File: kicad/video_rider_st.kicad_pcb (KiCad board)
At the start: 2 copper layers, 34 parts, among them J1 Conn_01x16_Female, J2 F3311A7H121020E200, J3 F3311A7H121020E200, J4 Conn_01x02_Male, J5 Conn_01x03_Male, J6 F3311A7H121020E200, J7 F3311A7H121020E200, J8 Conn_01x06_Male, U1 ST_SHIFTER_PHY, U10 ST_GLUE_PHY, U11 ST_GLUE_SOCKET, U2 ST_SHIFTER_SOCKET, U3 Pico, U4 74HC245, U5 74HC245, U6 74HC245, U7 74HC245, U8 LM1117-3.3, U9 XC95144XL-TQ100, X1 CXO_DIP14

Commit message: More layout experimentation
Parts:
- moved U6 37.0 mm to (185.2, 72.9)
- moved U7 23.1 mm to (177.3, 72.9)
- moved U2 8.60 mm to (198.2, 51.8)
- moved U4 3.76 mm to (155.8, 72.9)
- moved U5 3.55 mm to (163.7, 72.9)
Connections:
- net Net-(J5-Pad1) renamed /R_STE
- net Net-(J5-Pad2) renamed /G_STE
- net Net-(J5-Pad3) renamed /B_STE
- U6 pad 11: /B_OUT2 -> Net-(R2-Pad1)
- U6 pad 12: /B_OUT1 -> Net-(R3-Pad1)
- U6 pad 13: /B_OUT0 -> Net-(R4-Pad1)
- U6 pad 14: Net-(R3-Pad1) -> unconnected-(U6-Pad14)
- U6 pad 15: /G_OUT2 -> unconnected-(U6-Pad15)
- U6 pad 16: /G_OUT1 -> /B_OUT0
- U6 pad 17: /G_OUT0 -> /B_OUT1
- U6 pad 18: Net-(R2-Pad1) -> /B_OUT2
- U6 pad 2: /PICOG0 -> /PICOB3
- U6 pad 3: /PICOG1 -> /PICOB2
- U6 pad 4: /PICOG2 -> /PICOB1
- U6 pad 5: /PICOG3 -> unconnected-(U6-Pad5)
- U6 pad 6: /PICOB0 -> unconnected-(U6-Pad6)
- U6 pad 7: /PICOB1 -> /PICOB0
- U6 pad 8: /PICOB2 -> /PICOG0
- U6 pad 9: /PICOB3 -> /PICOR0
- U7 pad 11: unconnected-(U7-Pad11) -> /R_OUT0
- U7 pad 12: unconnected-(U7-Pad12) -> /R_OUT1
- U7 pad 13: unconnected-(U7-Pad13) -> /R_OUT2
- U7 pad 14: unconnected-(U7-Pad14) -> /G_OUT0
- U7 pad 15: /R_OUT2 -> /G_OUT1
- U7 pad 16: /R_OUT1 -> /G_OUT2
- U7 pad 17: /R_OUT0 -> unconnected-(U7-Pad17)
- U7 pad 18: Net-(R4-Pad1) -> unconnected-(U7-Pad18)
- U7 pad 19: /~{PICOEN_P} -> unconnected-(U7-Pad19)
- U7 pad 2: /PICOR0 -> unconnected-(U7-Pad2)
- U7 pad 3: /PICOR1 -> unconnected-(U7-Pad3)
- U7 pad 4: /PICOR2 -> /PICOG3
- U7 pad 5: /PICOR3 -> /PICOG2
- U7 pad 6: Net-(R1-Pad2) -> /PICOG1
- U7 pad 7: Net-(R1-Pad2) -> /PICOR3
- U7 pad 8: Net-(R1-Pad2) -> /PICOR2
- U7 pad 9: Net-(R1-Pad2) -> /PICOR1
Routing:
- net /G_OUT2: track 8.24 -> 28.9 mm
- net /B_OUT2: track 27.1 -> 47.7 mm
- net /G_OUT1: track 9.73 -> 27.1 mm
- net /B_OUT1: track 27.0 -> 43.4 mm
- net /G_OUT0: track 11.1 -> 25.1 mm
- net /R_OUT2: track 7.88 -> 20.3 mm
- net /B_OUT0: track 26.1 -> 38.2 mm
- net /XTL1: track 0.00 -> 12.0 mm
- net /XTL0: track 0.00 -> 12.0 mm
- net /SH_CS: track 0.00 -> 12.0 mm
- net /RW: track 0.00 -> 12.0 mm
- net /LOAD: track 0.00 -> 12.0 mm
- net /GND: track 0.00 -> 12.0 mm
- net /DE: track 0.00 -> 12.0 mm
- net /D9: track 0.00 -> 12.0 mm
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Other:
- board outline added: 51.9 x 39.6 mm

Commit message: Preliminary routeing of shifter board nearly complete
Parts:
- removed the C1 at (-11.3, 108.8)
- removed the C2 at (-11.3, 111.8)
- removed the J1 at (-71.2, 109.6)
- removed the U8 at (114.8, 126.0)
- added R2: 10k, Resistor_SMD:R_0805_2012Metric_Pad1.20x1.40mm_HandSolder, F.Cu at (193.2, 47.0)
- added R3: 10k, Resistor_SMD:R_0805_2012Metric_Pad1.20x1.40mm_HandSolder, F.Cu at (227.4, 56.0)
- C1: renamed from C3; moved to B.Cu
- C2: renamed from C4; moved to B.Cu
- C3: renamed from C5; moved to B.Cu
- C4: renamed from C6; moved to B.Cu
- C5: renamed from C7; moved to B.Cu
- D1: moved to B.Cu
- R7: renamed from R5; moved to B.Cu
- R8: renamed from R6; moved to B.Cu
- U10: renamed from U11; moved to B.Cu
- U9: renamed from U10; footprint Package_LCC:PLCC-68_THT-Socket -> PLCC_plugs:PLCC68_male_pins
- moved R6 270.5 mm to (240.8, 49.6), turned to -90 degrees
- moved R4 270.5 mm to (236.0, 49.6), turned to -90 degrees
- moved J4 262.9 mm to (232.6, 56.3), turned to 90 degrees
- moved R5 258.1 mm to (238.4, 49.6), turned to -90 degrees
- moved C1 254.5 mm to (109.0, 74.8), turned to -90 degrees
- moved J3 250.6 mm to (159.6, 82.5), turned to 180 degrees
- moved R1 247.2 mm to (212.6, 49.4)
- moved C3 245.6 mm to (105.0, 77.0), turned to -90 degrees
- moved C5 204.5 mm to (108.2, 88.0), turned to 90 degrees
- moved C2 183.3 mm to (76.8, 77.0)
- moved D1 160.0 mm to (149.8, 77.4), turned to 180 degrees
- moved C4 128.0 mm to (119.2, 84.8), turned to 90 degrees
- moved J2 119.7 mm to (247.3, 34.1), turned to 90 degrees
- moved J1 108.5 mm to (247.3, 48.1), turned to 90 degrees
- moved R8 104.7 mm to (84.8, 76.4), turned to -90 degrees
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- renumbered J2 to J1, J3 to J2, J4 to J3, J5 to J4, J6 to J5, J7 to J6, J8 to J7, R2 to R4, R3 to R5, R4 to R6, U9 to U8
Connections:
- J1 pad 10: /PICO_D4 -> /PICOG1
- J1 pad 11: /PICO_D3 -> /PICOG2
- J1 pad 12: /PICO_D2 -> /PICOG3
- J1 pad 13: /PICO_D1 -> /PICOB1
- J1 pad 14: /PICO_D0 -> /PICOB2
- J1 pad 15: /~{SHIFTEREN_P} -> /PICOB3
- J1 pad 16: /~{PICOEN_P} -> /PICOB0
- J1 pad 17: /PICOVSYNC -> /PICOG0
- J1 pad 18: /PICOHSYNC -> /PICOR0
- J1 pad 3: /PICO_A2 -> /~{PICOEN_P}
- J1 pad 4: /PICO_A1 -> /~{SHIFTEREN_P}
- J1 pad 5: /PICO_A0 -> unconnected-(J1-Pad5)
- J1 pad 6: /PICO_CLK -> unconnected-(J1-Pad6)
- J1 pad 7: /PICO_D7 -> /PICOR1
- J1 pad 8: /PICO_D6 -> /PICOR2
- J1 pad 9: /PICO_D5 -> /PICOR3
- J3 pad 2: /GND -> /GND_C
- J6 pad 10: /PICO_D4_C -> /PICOG3
- J6 pad 11: /PICO_D3_C -> /PICOB0
- J6 pad 12: /PICO_D2_C -> /PICOB1
- J6 pad 13: /PICO_D1_C -> /PICOB2
- J6 pad 14: /PICO_D0_C -> /PICOB3
- J6 pad 15: /~{SHIFTEREN_C} -> unconnected-(J6-Pad15)
- J6 pad 16: /~{PICOEN_C} -> unconnected-(J6-Pad16)
- J6 pad 17: /PICOVSYNC_C -> /~{SHIFTEREN_C}
- J6 pad 18: /PICOHSYNC_C -> /~{PICOEN_C}
- J6 pad 3: /PICO_A2_C -> /PICOR0
- J6 pad 4: /PICO_A1_C -> /PICOR1
- J6 pad 5: /PICO_A0_C -> /PICOR2
- J6 pad 6: /PICO_CLK_C -> /PICOR3
- J6 pad 7: /PICO_D7_C -> /PICOG0
- J6 pad 8: /PICO_D6_C -> /PICOG1
- J6 pad 9: /PICO_D5_C -> /PICOG2
- R1 pad 2: Net-(R1-Pad2) -> /5VPULL
- R4 pad 1: Net-(R2-Pad1) -> Net-(R4-Pad1)
- R5 pad 1: Net-(R3-Pad1) -> Net-(R5-Pad1)
- R6 pad 1: Net-(R4-Pad1) -> Net-(R6-Pad1)
- U3 pad 13: /GND -> /GND_C
- U3 pad 18: /GND -> /GND_C
- U3 pad 23: /GND -> /GND_C
- U3 pad 28: /GND -> /GND_C
- U3 pad 3: /GND -> /GND_C
- U3 pad 33: /GND -> /GND_C
- U3 pad 36: unconnected-(U3-Pad36) -> /3V3
- U3 pad 38: /GND -> /GND_C
- U3 pad 8: /GND -> /GND_C
- U4 pad 1: Net-(R1-Pad2) -> /5VPULL
- U4 pad 8: Net-(R1-Pad2) -> /5VPULL
- U4 pad 9: Net-(R1-Pad2) -> /5VPULL
- U5 pad 1: Net-(R1-Pad2) -> /5VPULL
- U5 pad 6: Net-(R1-Pad2) -> /5VPULL
- U5 pad 7: Net-(R1-Pad2) -> /5VPULL
- U5 pad 8: Net-(R1-Pad2) -> /5VPULL
- U5 pad 9: Net-(R1-Pad2) -> /5VPULL
- U6 pad 1: Net-(R1-Pad2) -> /5VPULL
- U6 pad 11: Net-(R2-Pad1) -> /B_OUT0
- U6 pad 12: Net-(R3-Pad1) -> /B_OUT1
- U6 pad 13: Net-(R4-Pad1) -> /B_OUT2
- U6 pad 16: /B_OUT0 -> Net-(R6-Pad1)
- U6 pad 17: /B_OUT1 -> Net-(R5-Pad1)
- U6 pad 18: /B_OUT2 -> Net-(R4-Pad1)
- U6 pad 2: /PICOB3 -> /PICOR0
- U6 pad 3: /PICOB2 -> /PICOG0
- U6 pad 4: /PICOB1 -> /PICOB0
- U6 pad 5: unconnected-(U6-Pad5) -> /5VPULL
- U6 pad 6: unconnected-(U6-Pad6) -> /5VPULL
- U6 pad 7: /PICOB0 -> /PICOB3
- U6 pad 8: /PICOG0 -> /PICOB2
- U6 pad 9: /PICOR0 -> /PICOB1
- U7 pad 1: Net-(R1-Pad2) -> /5VPULL
- U7 pad 19: unconnected-(U7-Pad19) -> /~{PICOEN_P}
- U7 pad 2: unconnected-(U7-Pad2) -> /5VPULL
- U7 pad 3: unconnected-(U7-Pad3) -> /5VPULL
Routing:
- net /FCS: track 0.00 -> 117.5 mm
- net /DEV: track 0.00 -> 116.2 mm
- net /DMA: track 0.00 -> 111.1 mm
- net /RAM: track 0.00 -> 109.9 mm
- net /RESET: track 0.00 -> 104.7 mm
- net /ROM0: track 0.00 -> 103.6 mm
- net /ROM1: track 0.00 -> 98.3 mm
- net /ROM2: track 0.00 -> 97.1 mm
- net /ROM3: track 0.00 -> 92.0 mm
- net /ROM4: track 0.00 -> 90.4 mm
- net /VMA: track 0.00 -> 85.7 mm
- net /FC0: track 0.00 -> 83.3 mm
- net /5V: track 12.0 -> 94.9 mm, vias 0 -> 8
- net /FC1: track 0.00 -> 79.4 mm
- net /FC2: track 0.00 -> 75.2 mm
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- added copper zone on F.Cu, net /GND
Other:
- board size 51.9 x 39.6 mm -> 193.9 x 104.1 mm

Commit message: Basic board outline and routeing done. Need sanity and DRC check
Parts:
- J3: footprint Connector_PinHeader_2.54mm:PinHeader_1x02_P2.54mm_Vertical -> Connector_PinHeader_2.54mm:PinHeader_1x02_P2.54mm_Horizontal
- J4: footprint Connector_PinHeader_2.54mm:PinHeader_1x03_P2.54mm_Horizontal -> Connector_PinHeader_2.54mm:PinHeader_1x03_P2.54mm_Vertical
- J7: footprint Connector_PinHeader_2.54mm:PinHeader_1x06_P2.54mm_Horizontal -> Connector_PinHeader_2.54mm:PinHeader_1x06_P2.54mm_Vertical
- R1, R2, R3: value 10k -> 6k8
- moved R7 176.5 mm to (169.4, 88.5)
- moved J7 173.5 mm to (170.5, 90.7)
- moved J2 110.9 mm to (144.7, 75.9), turned to -90 degrees
- moved U2 108.4 mm to (150.4, 84.3), turned to 90 degrees
- moved J1 103.6 mm to (144.7, 61.9), turned to -90 degrees
- moved U1 97.5 mm to (150.4, 72.3), turned to 90 degrees
- moved R6 90.2 mm to (151.2, 60.4), turned to 90 degrees
- moved R5 85.5 mm to (153.6, 60.4), turned to 90 degrees
- moved R4 80.7 mm to (156.0, 60.4), turned to 90 degrees
- moved J4 73.3 mm to (159.4, 53.7), turned to -90 degrees
- moved U6 67.1 mm to (163.5, 63.2), turned to 90 degrees
- moved D1 66.8 mm to (174.4, 139.5)
- moved J6 64.6 mm to (186.5, 88.4)
- moved R3 62.8 mm to (164.6, 54.0), turned to 180 degrees
- moved R8 56.1 mm to (134.6, 102.2)
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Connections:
- D1 pad 2: /5V -> /5V_C
- J6 pad 10: /PICOG3 -> /PICOG1_C
- J6 pad 11: /PICOB0 -> /PICOG2_C
- J6 pad 12: /PICOB1 -> /PICOG3_C
- J6 pad 13: /PICOB2 -> /PICOB1_C
- J6 pad 14: /PICOB3 -> /PICOB2_C
- J6 pad 15: unconnected-(J6-Pad15) -> /PICOB3_C
- J6 pad 16: unconnected-(J6-Pad16) -> /PICOB0_C
- J6 pad 17: /~{SHIFTEREN_C} -> /PICOG0_C
- J6 pad 18: /~{PICOEN_C} -> /PICOR0_C
- J6 pad 3: /PICOR0 -> /~{PICOEN_C}
- J6 pad 4: /PICOR1 -> /~{SHIFTEREN_C}
- J6 pad 5: /PICOR2 -> unconnected-(J6-Pad5)
- J6 pad 6: /PICOR3 -> unconnected-(J6-Pad6)
- J6 pad 7: /PICOG0 -> /PICOR1_C
- J6 pad 8: /PICOG1 -> /PICOR2_C
- J6 pad 9: /PICOG2 -> /PICOR3_C
- U1 pad 32: /A5 -> /A5_S
- U1 pad 33: /A4 -> /A4_S
- U1 pad 34: /A3 -> /A3_S
- U1 pad 35: /A2 -> /A2_S
- U1 pad 36: /A1 -> /A1_S
- U10 pad 39: /DE -> /DE_C
- U10 pad 48: /D0 -> /D0_G
- U10 pad 49: /D1 -> /D1_G
- U10 pad 55: /RW -> /RW_C
- U2 pad 32: /A5 -> /A5_S
- U2 pad 33: /A4 -> /A4_S
- U2 pad 34: /A3 -> /A3_S
- U2 pad 35: /A2 -> /A2_S
- U2 pad 36: /A1 -> /A1_S
- U3 pad 1: /PICOR0 -> /PICOR0_C
- U3 pad 10: /PICOG3 -> /PICOG3_C
- U3 pad 11: /PICOB0 -> /PICOB0_C
- U3 pad 12: /PICOB1 -> /PICOB1_C
- U3 pad 14: /PICOB2 -> /PICOB2_C
- U3 pad 15: /PICOB3 -> /PICOB3_C
- U3 pad 2: /PICOR1 -> /PICOR1_C
- U3 pad 4: /PICOR2 -> /PICOR2_C
- U3 pad 5: /PICOR3 -> /PICOR3_C
- U3 pad 6: /PICOG0 -> /PICOG0_C
- U3 pad 7: /PICOG1 -> /PICOG1_C
- U3 pad 9: /PICOG2 -> /PICOG2_C
- U8 pad 10: /BLANK_OUT -> /A2
- U8 pad 11: /RW -> /A3
- U8 pad 12: /AS -> /A4
- U8 pad 13: /LDS -> /A5
- U8 pad 14: /UDS -> /A6
- U8 pad 15: /DTACK -> /A7
- U8 pad 16: unconnected-(U8-Pad16) -> /RW_C
- U8 pad 17: unconnected-(U8-Pad17) -> /A9
- U8 pad 18: unconnected-(U8-Pad18) -> /A8
- U8 pad 19: unconnected-(U8-Pad19) -> /LDS
- U8 pad 20: unconnected-(U8-Pad20) -> /UDS
- U8 pad 22: /8MHZ -> /OSC
- U8 pad 23: /OSC -> /HSYNC
- U8 pad 24: unconnected-(U8-Pad24) -> /VSYNC
- U8 pad 25: unconnected-(U8-Pad25) -> /BLANK
- U8 pad 27: unconnected-(U8-Pad27) -> /8MHZ
- U8 pad 28: /PICO_A2_C -> /A12
- U8 pad 29: /PICO_A1_C -> /A13
- U8 pad 30: /PICO_A0_C -> /A10
- U8 pad 32: /PICO_CLK_C -> /A11
- U8 pad 33: /PICO_D7_C -> /A14
- U8 pad 34: /PICO_D6_C -> /A15
- U8 pad 35: /A23 -> /A16
- U8 pad 36: /A22 -> /A17
- U8 pad 37: /A21 -> /A18
- U8 pad 39: /A20 -> /A19
- U8 pad 4: /VSYNC -> /BLANK_OUT
- U8 pad 40: /A19 -> /A20
- U8 pad 41: /A18 -> /A21
- U8 pad 42: /A17 -> /A23
- U8 pad 43: /A16 -> /A22
- U8 pad 46: /A15 -> /AS
- U8 pad 49: /A14 -> /DTACK
- U8 pad 50: /A3 -> unconnected-(U8-Pad50)
- U8 pad 52: /A2 -> unconnected-(U8-Pad52)
- U8 pad 53: /A1 -> unconnected-(U8-Pad53)
- U8 pad 55: /D0_C -> /PICO_A2
- U8 pad 56: /D1_C -> /PICO_A1
- U8 pad 58: /D2_C -> /PICO_A0
- U8 pad 59: /D3_C -> /PICO_CLK
- U8 pad 6: /HSYNC -> /HSYNC_OUT
- U8 pad 60: /D4_C -> /PICO_D7
- U8 pad 61: /D5_C -> /PICO_D6
- U8 pad 63: /D6_C -> /PICO_D5
- U8 pad 64: /D7_C -> /PICO_D4
- U8 pad 65: /D8_C -> /PICOVSYNC
- U8 pad 66: /D9_C -> /PICOHSYNC
- U8 pad 67: /D10_C -> /PICO_D0
- U8 pad 68: /D11_C -> /PICO_D1
- U8 pad 70: /D12_C -> /PICO_D3
- U8 pad 71: /D13_C -> /PICO_D2
- U8 pad 72: /D14_C -> /~{SHIFTEREN_C}
- U8 pad 73: /D15_C -> /~{PICOEN_C}
- U8 pad 74: /A13 -> unconnected-(U8-Pad74)
- U8 pad 76: /A12 -> /D0_C
- U8 pad 77: /A11 -> /D1_C
- U8 pad 78: /A10 -> /D2_C
- U8 pad 79: /A9 -> /D3_C
- U8 pad 8: /HSYNC_OUT -> unconnected-(U8-Pad8)
- U8 pad 80: /A8 -> /D4_C
- U8 pad 81: /A7 -> /D5_C
- U8 pad 82: /A6 -> /D6_C
- U8 pad 85: /A5 -> /D7_C
- U8 pad 86: /A4 -> /D8_C
- U8 pad 87: /PICO_D5_C -> /D9_C
- U8 pad 89: /PICO_D4_C -> /D10_C
- U8 pad 9: /BLANK -> /A1
- U8 pad 90: /PICO_D3_C -> /D11_C
- U8 pad 91: /PICO_D2_C -> /D12_C
- U8 pad 92: /PICO_D1_C -> /D13_C
- U8 pad 93: /PICO_D0_C -> /D14_C
- U8 pad 94: /~{SHIFTEREN_C} -> /D15_C
- U8 pad 95: /~{PICOEN_C} -> unconnected-(U8-Pad95)
- U8 pad 96: /PICOVSYNC_C -> unconnected-(U8-Pad96)
- U8 pad 97: /PICOHSYNC_C -> unconnected-(U8-Pad97)
- U9 pad 39: /DE -> /DE_C
- U9 pad 48: /D0 -> /D0_G
- U9 pad 49: /D1 -> /D1_G
- U9 pad 55: /RW -> /RW_C
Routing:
- net /5V_C: track 36.9 -> 185.8 mm, vias 0 -> 4
- net /3V3: track 0.00 -> 112.8 mm, vias 0 -> 6
- net /BLANK_OUT: track 0.00 -> 99.6 mm, vias 0 -> 1
- net /HSYNC_OUT: track 0.00 -> 98.8 mm, vias 0 -> 1
- net /VSYNC_OUT: track 0.00 -> 98.8 mm, vias 0 -> 1
- net /~{SHIFTEREN_P}: track 0.00 -> 81.7 mm, vias 0 -> 4
- net /PICOR0_C: track 0.00 -> 67.7 mm, vias 0 -> 2
- net /PICOR1_C: track 0.00 -> 57.2 mm, vias 0 -> 2
- net /PICOG0_C: track 0.00 -> 56.8 mm, vias 0 -> 2
- net /DEV: track 116.2 -> 61.1 mm, vias 0 -> 1
- net /PICOR2_C: track 0.00 -> 54.9 mm, vias 0 -> 2
- net /FCS: track 117.5 -> 63.1 mm, vias 0 -> 1
- net /PICOR3_C: track 0.00 -> 50.7 mm, vias 0 -> 2
- net /PICOG1_C: track 0.00 -> 48.8 mm, vias 0 -> 2
- net /RAM: track 109.9 -> 63.0 mm, vias 0 -> 1
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- added copper zone on B.Cu, net /GND_C
- added copper zone on F.Cu, net /GND_C
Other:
- board size 193.9 x 104.1 mm -> 104 x 92.1 mm

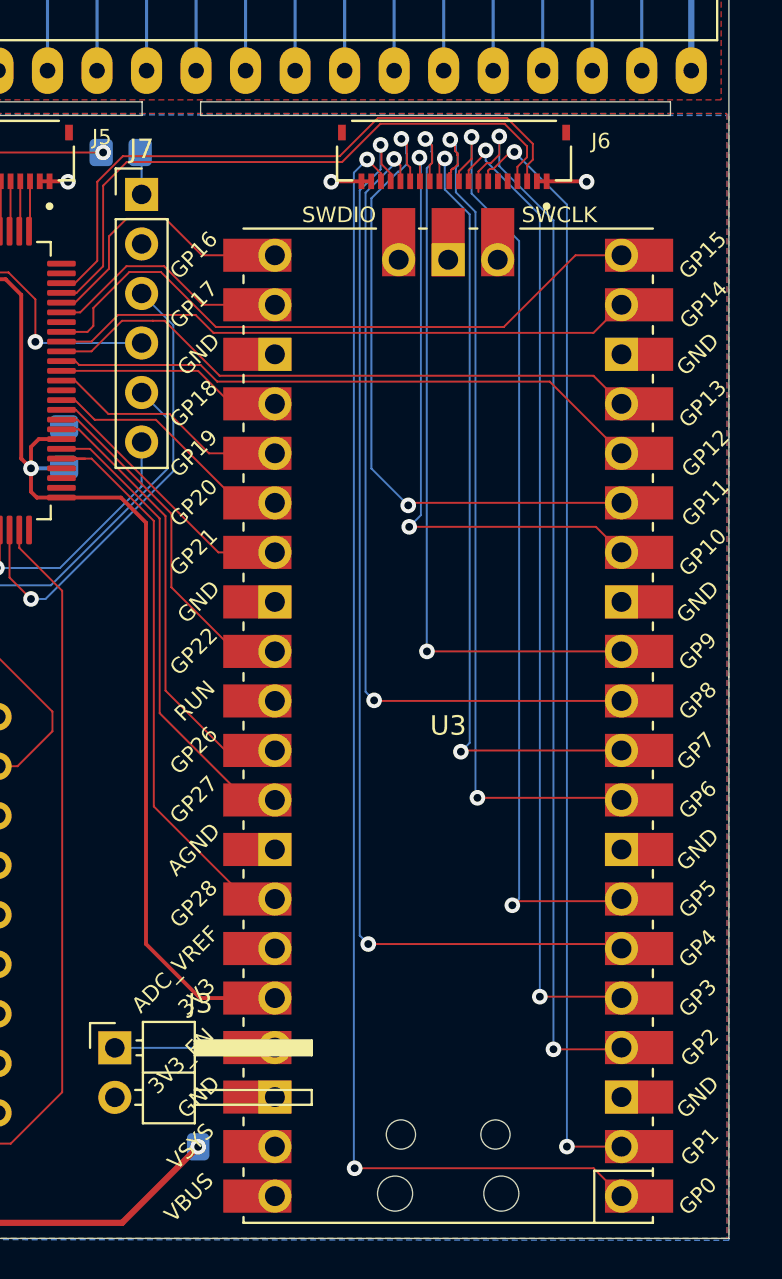
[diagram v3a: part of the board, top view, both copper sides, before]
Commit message: Rerouteing pico to bottom layer
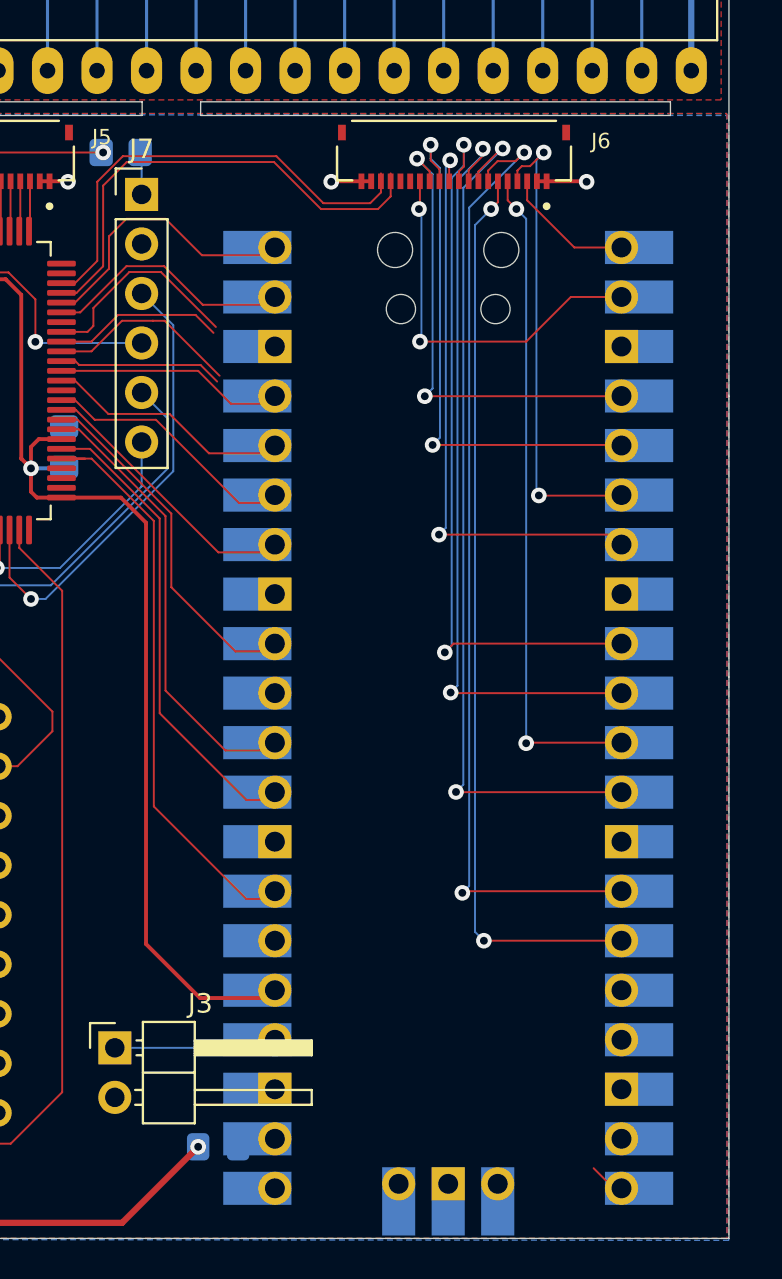
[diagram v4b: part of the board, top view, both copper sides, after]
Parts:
- U3: moved to B.Cu
- moved U3 0.40 mm to (186.2, 117.5)
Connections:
- J5 pad 10: /D7_C -> /D8_C
- J5 pad 11: /D8_C -> /D7_C
- J5 pad 12: /D9_C -> /D6_C
- J5 pad 13: /D10_C -> /D5_C
- J5 pad 14: /D11_C -> /D4_C
- J5 pad 15: /D12_C -> /D3_C
- J5 pad 16: /D13_C -> /D2_C
- J5 pad 17: /D14_C -> /D1_C
- J5 pad 18: /D15_C -> /D0_C
- J5 pad 3: /D0_C -> /D15_C
- J5 pad 4: /D1_C -> /D14_C
- J5 pad 5: /D2_C -> /D13_C
- J5 pad 6: /D3_C -> /D12_C
- J5 pad 7: /D4_C -> /D11_C
- J5 pad 8: /D5_C -> /D10_C
- J5 pad 9: /D6_C -> /D9_C
- J6 pad 10: /PICOG1_C -> /PICOG2_C
- J6 pad 11: /PICOG2_C -> /PICOG1_C
- J6 pad 12: /PICOG3_C -> /PICOR3_C
- J6 pad 13: /PICOB1_C -> /PICOR2_C
- J6 pad 14: /PICOB2_C -> /PICOR1_C
- J6 pad 15: /PICOB3_C -> unconnected-(J6-Pad15)
- J6 pad 16: /PICOB0_C -> unconnected-(J6-Pad16)
- J6 pad 17: /PICOG0_C -> /~{SHIFTEREN_C}
- J6 pad 18: /PICOR0_C -> /~{PICOEN_C}
- J6 pad 3: /~{PICOEN_C} -> /PICOR0_C
- J6 pad 4: /~{SHIFTEREN_C} -> /PICOG0_C
- J6 pad 5: unconnected-(J6-Pad5) -> /PICOB0_C
- J6 pad 6: unconnected-(J6-Pad6) -> /PICOB3_C
- J6 pad 7: /PICOR1_C -> /PICOB2_C
- J6 pad 8: /PICOR2_C -> /PICOB1_C
- J6 pad 9: /PICOR3_C -> /PICOG3_C
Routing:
- net /PICOR0_C: track 67.7 -> 6.82 mm, vias 2 -> 0
- net /PICOR1_C: track 57.2 -> 19.6 mm
- net /PICOG0_C: track 56.8 -> 24.3 mm
- net /PICOR2_C: track 54.9 -> 24.3 mm
- net /PICOR3_C: track 50.7 -> 27.5 mm
- net unconnected-(U3-Pad30): track 0.00 -> 23.0 mm
- net /PICO_A0: track 23.0 -> 0.00 mm
- net /PICOVSYNC: track 30.7 -> 8.52 mm
- net /PICO_D0: track 30.3 -> 8.75 mm
- net /PICOHSYNC: track 31.1 -> 10.1 mm
- net /PICO_D1: track 33.2 -> 12.9 mm
- net /PICOG1_C: track 48.8 -> 30.1 mm
- net /PICOB2_C: track 31.9 -> 50.4 mm
- net /PICO_D7: track 14.0 -> 30.1 mm
- net /PICO_A2: track 30.1 -> 14.0 mm
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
